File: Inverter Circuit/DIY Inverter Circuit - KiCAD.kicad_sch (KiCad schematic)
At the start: 9 parts, among them J1 EGS002 Pinout, J2 Battery Input, Q1 FQP90N03, SW1 ON/OFF Switch, U1 L7805

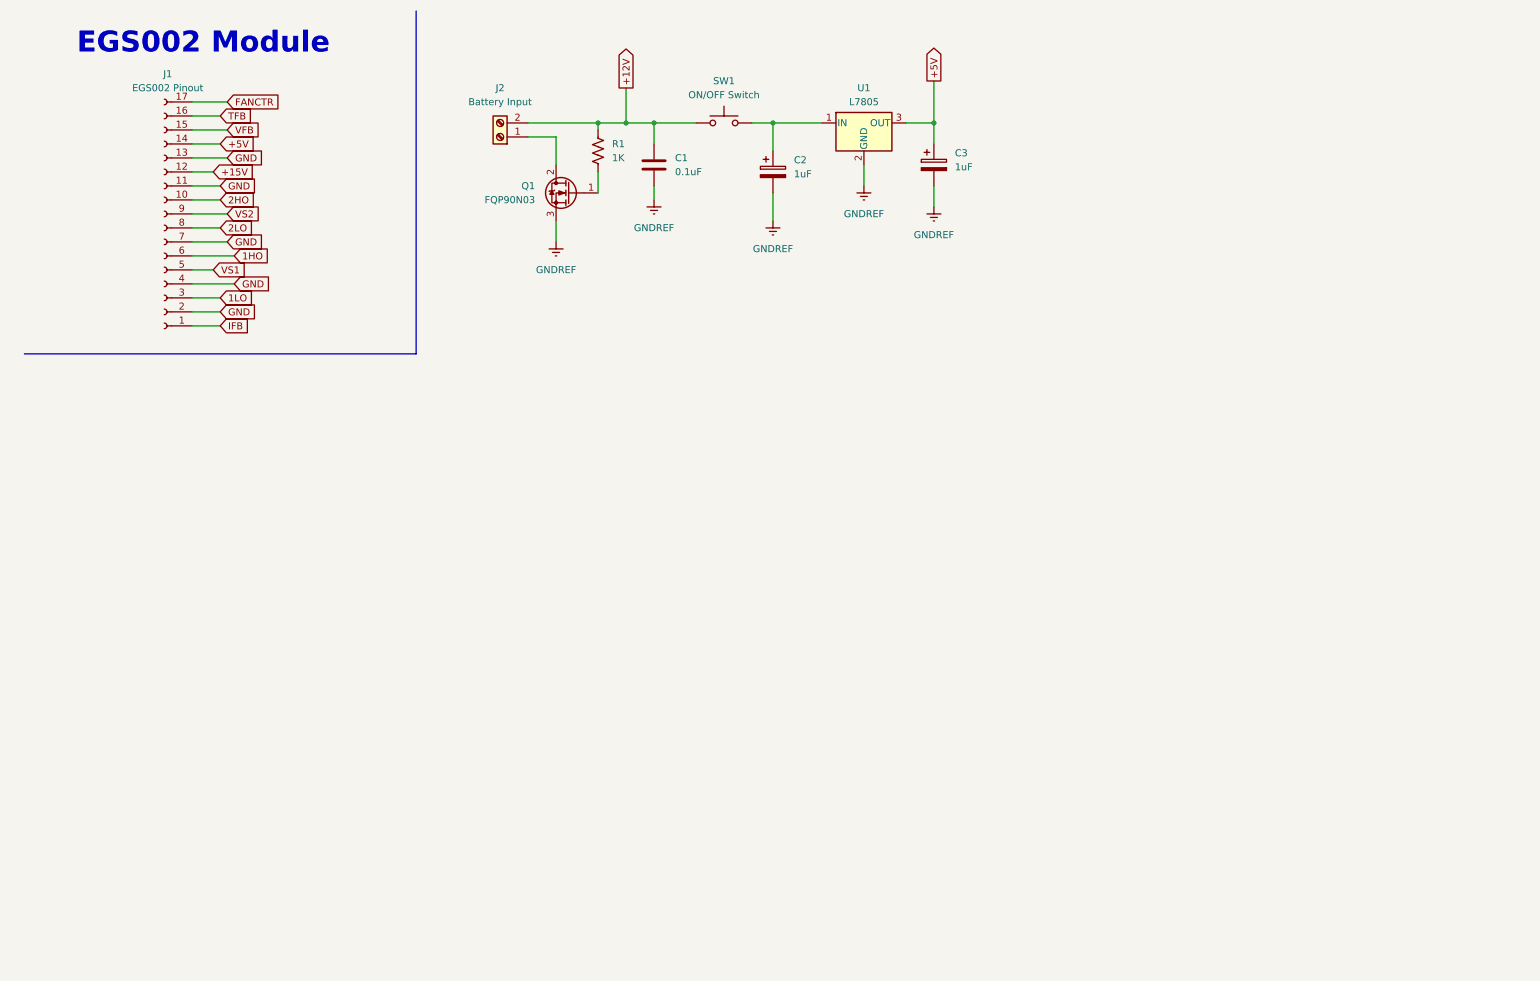
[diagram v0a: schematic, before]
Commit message: GUI BugFixes
- uploaded the right Gui.py (forgot to upload it lol)
- added the AR and EN in the Gui.py can be changed manually  (for now)
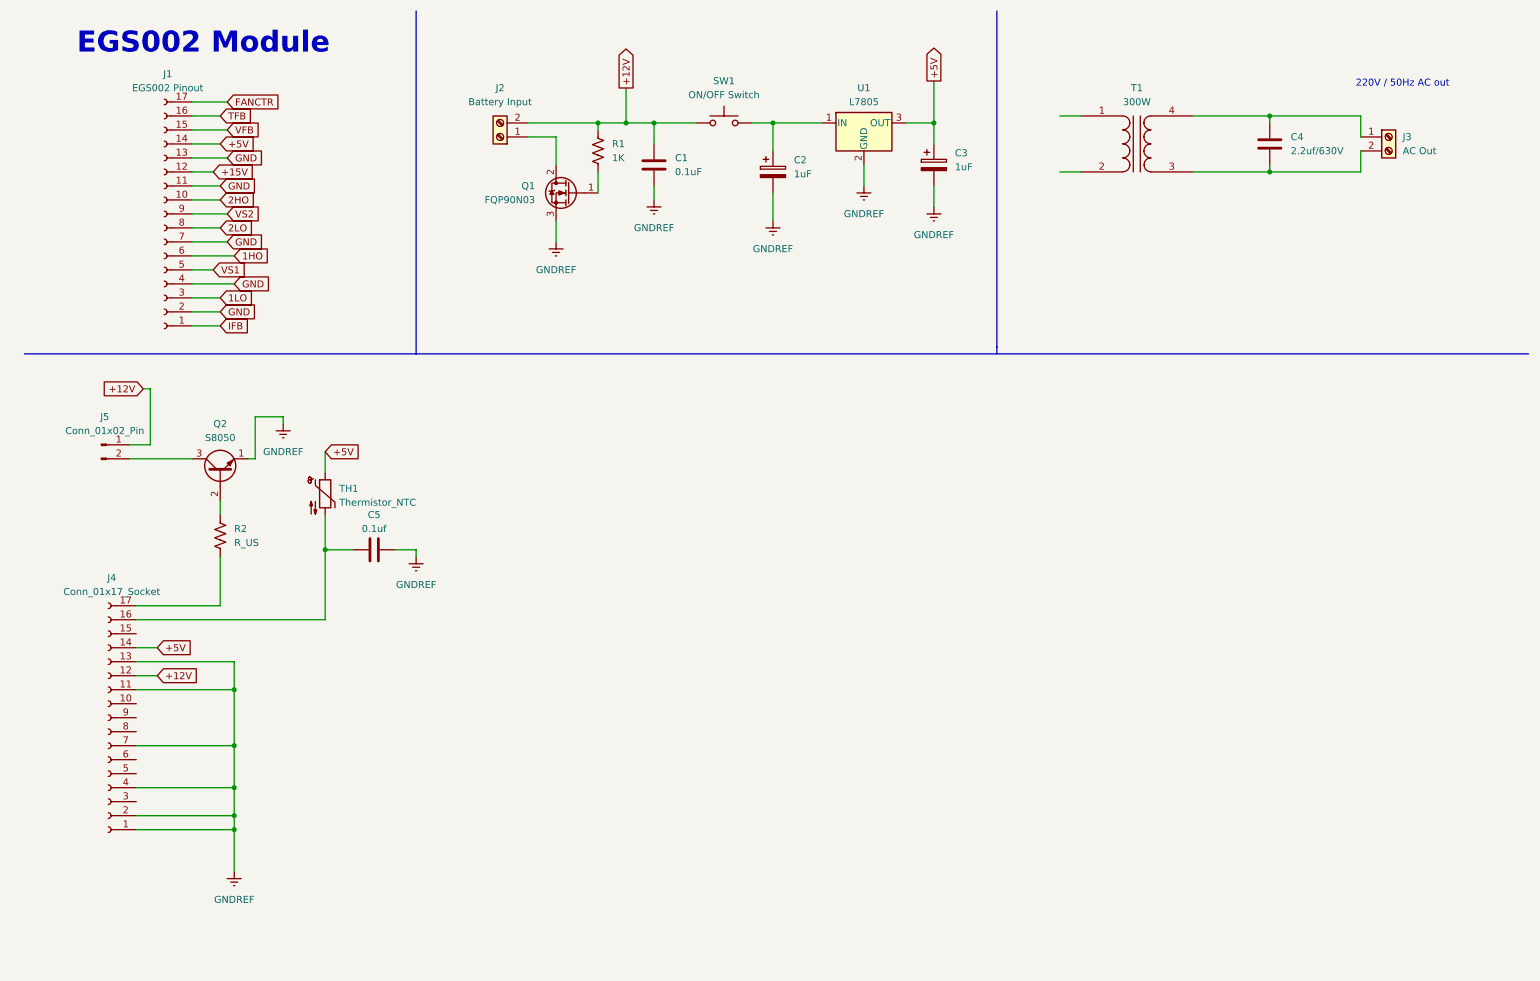
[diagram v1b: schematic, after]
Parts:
- added C4: 2.2uf/630V, symbol Device:C
- added C5: 0.1uf, symbol Device:C
- added J3: AC Out, symbol Connector:Screw_Terminal_01x02
- added J4: Conn_01x17_Socket, symbol Connector:Conn_01x17_Socket
- added J5: Conn_01x02_Pin, symbol Connector:Conn_01x02_Pin
- added Q2: S8050, Package_TO_SOT_THT:TO-92_Inline, symbol Transistor_BJT:S8050
- added R2: R_US, symbol Device:R_US
- added T1: 300W, symbol Device:Transformer_1P_1S
- added TH1: Thermistor_NTC, symbol Device:Thermistor_NTC
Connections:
- net +12V: now also J4.12 (Pin_12), J5.1 (Pin_1)
- net +5V: now also J4.14 (Pin_14), TH1.1
- net GNDREF: now also C5.1, J4.1 (Pin_1), J4.11 (Pin_11), J4.13 (Pin_13), J4.2 (Pin_2), J4.4 (Pin_4), J4.7 (Pin_7), Q2.1 (E)
- new net: Q2.2 (B), R2.2
- new net: J5.2 (Pin_2), Q2.3 (C)
- new net: C4.1, J3.1 (Pin_1), T1.4 (SB)
- new net: C4.2, J3.2 (Pin_2), T1.3 (SA)
- new net: J4.17 (Pin_17), R2.1
- new net: C5.2, J4.16 (Pin_16), TH1.2
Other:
- note added: "220V / 50Hz AC out"

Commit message: Inverter Circuito
Routed
comps layed
3D model inspected
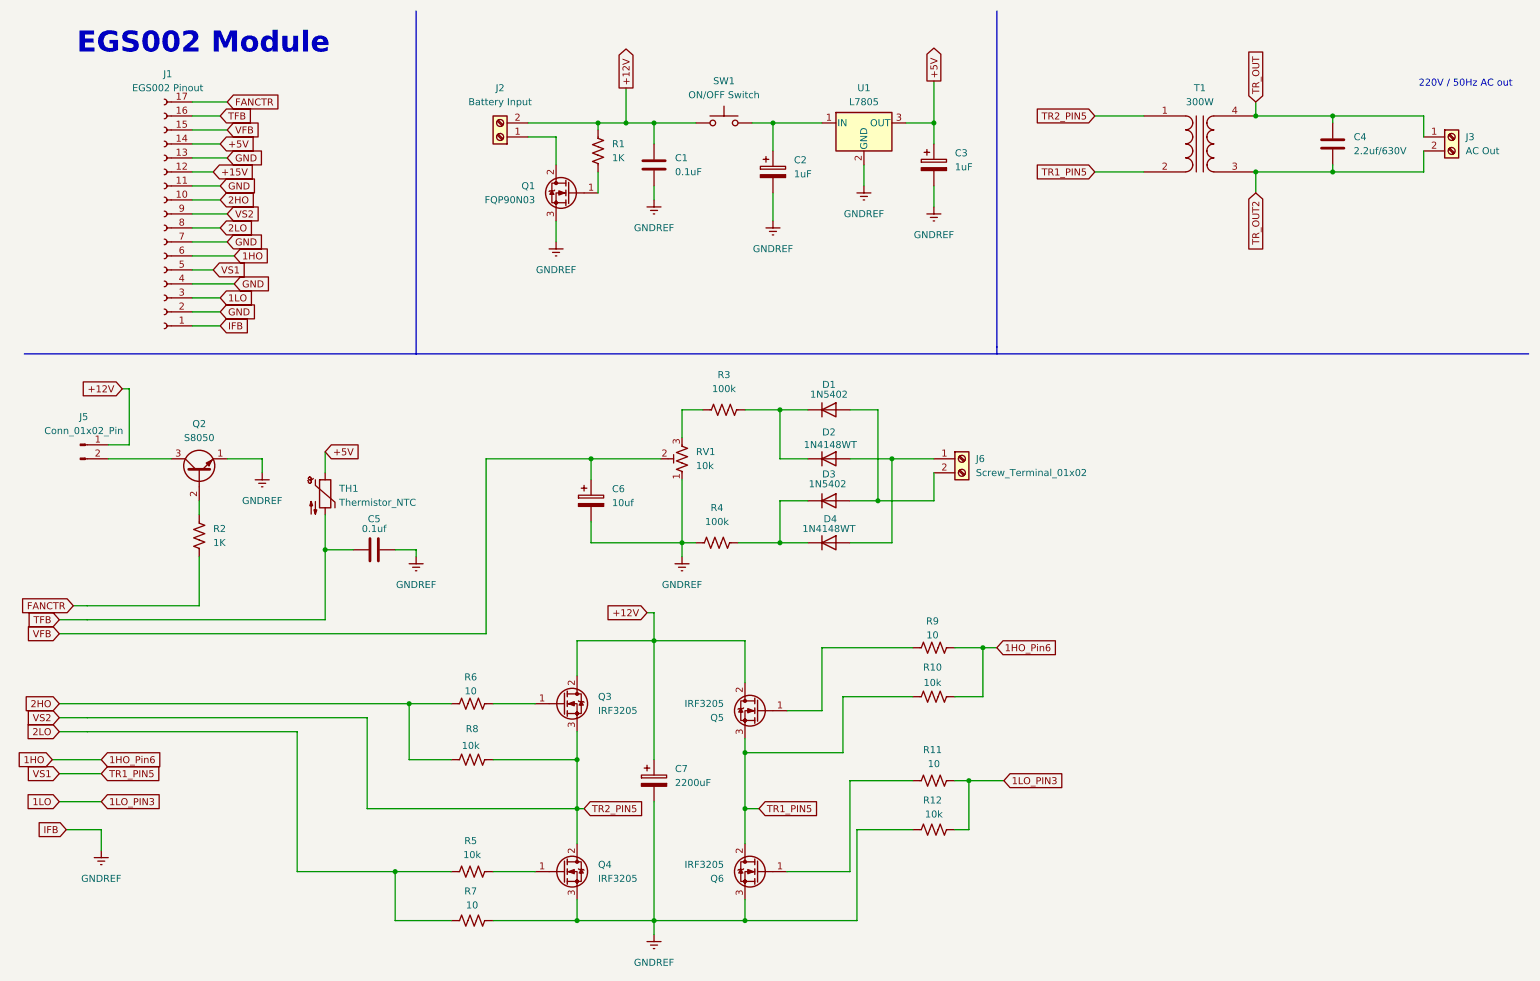
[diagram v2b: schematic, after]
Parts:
- removed J4: Conn_01x17_Socket, symbol Connector:Conn_01x17_Socket
- added C6: 10uf, Capacitor_THT:CP_Radial_D10.0mm_P7.50mm, symbol Device:C_Polarized
- added C7: 2200uF, Capacitor_THT:CP_Radial_D16.0mm_P7.50mm, symbol Device:C_Polarized
- added D1, D3: 1N5402, Diode_THT:D_A-405_P10.16mm_Horizontal, symbol Diode:1N5402
- added D2, D4: 1N4148WT, Diode_THT:D_A-405_P10.16mm_Horizontal, symbol Diode:1N4148WT
- added J6: Screw_Terminal_01x02, TerminalBlock_Phoenix:TerminalBlock_Phoenix_MKDS-1,5-2_1x02_P5.00mm_Horizontal, symbol Connector:Screw_Terminal_01x02
- added Q3, Q4, Q5, Q6: IRF3205, Package_TO_SOT_THT:TO-220-3_Vertical, symbol Transistor_FET:IRF3205
- added R10, R12, R5, R8: 10k, Resistor_THT:R_Axial_DIN0204_L3.6mm_D1.6mm_P7.62mm_Horizontal, symbol Device:R_US
- added R11, R6, R7, R9: 10, Resistor_THT:R_Axial_DIN0204_L3.6mm_D1.6mm_P7.62mm_Horizontal, symbol Device:R_US
- added R3, R4: 100k, Resistor_THT:R_Axial_DIN0204_L3.6mm_D1.6mm_P7.62mm_Horizontal, symbol Device:R_US
- added RV1: 10k, Potentiometer_THT:Potentiometer_Vishay_T93XA_Horizontal, symbol Device:R_Potentiometer_Trim_US
- C4: footprint (none) -> Capacitor_THT:C_Rect_L26.5mm_W6.0mm_P22.50mm_MKS4
- C5: footprint (none) -> Capacitor_THT:C_Disc_D3.0mm_W1.6mm_P2.50mm
- J3, J5, T1: footprint (none) -> TerminalBlock_Phoenix:TerminalBlock_Phoenix_MKDS-1,5-2_1x02_P5.00mm_Horizontal
- R2: value R_US -> 1K; footprint (none) -> Resistor_THT:R_Axial_DIN0204_L3.6mm_D1.6mm_P7.62mm_Horizontal
- TH1: footprint (none) -> Resistor_THT:R_Axial_DIN0614_L14.3mm_D5.7mm_P5.08mm_Vertical
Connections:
- net IFB is gone; now on net GNDREF: J1.1 (Pin_1)
- net VS1 is gone; now on net TR1_PIN5: J1.5 (Pin_5)
- net VS2 is gone; now on net TR2_PIN5: J1.9 (Pin_9)
- net +12V: now also C7.1, Q3.2 (D), Q5.2 (D)
- net 1HO: now also R10.2, R9.2
- net 1LO: now also R11.1, R12.1
- net 2HO: now also R6.1, R8.1
- net 2LO: now also R5.2, R7.2
- net FANCTR: now also R2.1
- net GNDREF: now also C6.2, C7.2, Q4.3 (S), Q6.3 (S), R12.2, R4.2, R7.1, RV1.1
- net TFB: now also C5.2, TH1.2
- net VFB: now also C6.1, RV1.2
- net TR_OUT: now reaches C4.1, J3.1 (Pin_1), T1.4 (SB)
- net TR_OUT2: now reaches C4.2, J3.2 (Pin_2), T1.3 (SA)
- net TR2_PIN5: now reaches T1.1 (AA)
- net TR2_PIN5: now also Q3.3 (S), Q4.2 (D), R8.2
- net TR1_PIN5: now reaches T1.2 (AB)
- net TR1_PIN5: now also Q5.3 (S), Q6.2 (D), R10.1
- new net: Q5.1 (G), R9.1
- new net: Q3.1 (G), R6.2
- new net: D1.1 (K), D2.1 (K), R3.2
- new net: D2.2 (A), D4.2 (A), J6.1 (Pin_1)
- new net: D3.1 (K), D4.1 (K), R4.1
- new net: R3.1, RV1.3
- new net: Q4.1 (G), R5.1
- new net: Q6.1 (G), R11.2
- new net: D1.2 (A), D3.2 (A), J6.2 (Pin_2)
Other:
- moved on the sheet: C4, J3, J5, Q2, R2, T1
